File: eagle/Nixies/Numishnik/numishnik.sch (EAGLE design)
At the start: 74 parts, among them IC2 78L05F, IC5 74141N, IC6 DS3234, IC7 MEGA8-AI, Q1 IRF630N, SW1 BUTTON-IT_1181, T1 BTA92, T13 BTA42, T2 BTA42, T3 BTA92, T4 BTA42, T5 BTA92, T6 BTA42, T7 BTA92, T8 BTA42, X3 53047-06

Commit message: added IV-16 Numishnik
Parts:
- removed 220: (no value), rcl:CPOL-EUD/7343-31R
- removed C10: 10uF, rcl:CPOL-EUSMCB
- removed C100: 10uF/250V, rcl:CPOL-EUE5-13
- removed C12: 1.0, rcl:C-EUC0805S
- removed C6: 100/24V, rcl:CPOL-EUE3.5-8
- removed DOT1, DOT2, PAD1, PAD2: (no value), wirepad:1,6/0,8
- removed IC5: 74141N, 74xx-eu:74141N
- removed J2: (no value), 0-svo:DCJ-SMALL
- removed Q1: IRF630N, transistor-power:IRF740
- removed R14: (no value), 0-svo:RES4
- removed R18, R22, R26, R30: 2.4K, rcl:R-EU_R0805S
- removed R19, R23, R27, R31: 27K, rcl:R-EU_R0805S
- removed R21, R25, R29: 91K, rcl:R-EU_R0805S
- removed R4: 000, rcl:R-EU_R0805S
- removed S1, S2: (no value), switch-omron:31-XX
- removed SV1, SV2: (no value), con-lsta:FE20-1
- removed T1, T3, T5, T7: BTA92, transistor:MMBTA92LT1-PNP-SOT23-BEC
- removed T13, T2, T4, T6, T8: BTA42, transistor:MMBTA42LT1-NPN-SOT23-BEC
- removed U$1, U$2, U$3, U$4: IN-14, 0-nixies-russian:IN-14
- added C3: 10uF, rcl:CPOL-EUSMCB
- added IC1: MBI5026GP, 0-macroblock:MBI5026GP
- added N1, N2, N3, N4: IV-16, 0-nixies-russian:IV-16
- added R12, R13: 000, rcl:R-EU_R0805S
- added TP1, TP2: TPSPAD1-13, 0-svo:TPSPAD1-13
- added X1: USB-MICROB, SparkFun:USB-MICROB
- C2: value 33nF -> 10uF; device rcl:C-EUC0805S -> rcl:CPOL-EUSMCB
- D1: value 31DF6 -> BZX84C 3.3V; device diode:RGP30 -> diode:BZX84CSMD
- D2: value BAT54C -> BZX84C 3.3V; device diode:DIODE-2AC|CASOT23 -> diode:BZX84CSMD
- D3: value BAT54S -> 1N4004; device diode:DIODE_2CACA-SOT23 -> diode:1N4004
- IC2: value 78L05F -> MBI5026GP; device linear:78L05F -> 0-macroblock:MBI5026GP
- R1: value 91K -> 820
- R10: value 27K -> 10
- R11, R7, R8: value 1K -> 10
- R17: value 91K -> 2K2
- R2: value 470K -> 820
- R3: value 4K7 -> 100
- R6, R9: value 1K -> 100
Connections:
- net N$53 renamed RTCVCC
- removed net +UB: C6.+, IC2.VI, J2.1, PAD2.P
- removed net C0: IC5A.0, SV1.1, SV2.1, U$1.0, U$2.0, U$3.0, U$4.0
- removed net C1: IC5A.1, SV1.2, SV2.2, U$1.1, U$2.1, U$3.1, U$4.1
- removed net C2: IC5A.2, SV1.3, SV2.3, U$1.2, U$2.2, U$3.2, U$4.2
- removed net C3: IC5A.3, SV1.4, SV2.4, U$1.3, U$2.3, U$3.3, U$4.3
- removed net C4: IC5A.4, SV1.5, SV2.5, U$1.4, U$2.4, U$3.4, U$4.4
- removed net C5: IC5A.5, SV1.16, SV2.16, U$1.5, U$2.5, U$3.5, U$4.5
- removed net C6: IC5A.6, SV1.17, SV2.17, U$1.6, U$2.6, U$3.6, U$4.6
- removed net C7: IC5A.7, SV1.18, SV2.18, U$1.7, U$2.7, U$3.7, U$4.7
- removed net C8: IC5A.8, SV1.19, SV2.19, U$1.8, U$2.8, U$3.8, U$4.8
- removed net C9: IC5A.9, SV1.20, SV2.20, U$1.9, U$2.9, U$3.9, U$4.9
- removed net D0: IC5A.A, IC7.PC3(ADC3)
- removed net D1: IC5A.B, IC7.PC1(ADC1)
- removed net D2: IC5A.C, IC7.PC0(ADC0)
- removed net D3: IC5A.D, IC7.PC2(ADC2)
- removed net FBACK: C12.1, D3.AC, IC7.ADC7, R2.2, R3.2
- removed net HV+: C100.+, D1.C, R10.2, R18.2, R2.1, R22.2, R26.2, R30.2, SV1.6, SV2.6, T1.E, T3.E, T5.E, T7.E
- removed net HVPUMP: C2.2, IC7.PB1(OC1A)
- removed net N$10 (its old number): R19.1, U$1.A
- removed net N$15: R9.2, T6.B
- removed net N$16: R25.2, R26.1, T5.B
- removed net N$17: R25.1, T6.C
- removed net N$18: R27.2, T5.C
- removed net N$19: R23.1, U$2.A
- removed net N$20: R11.2, T8.B
- removed net N$21: R6.1, T13.B
- removed net N$22: R29.2, R30.1, T7.B
- removed net N$23: R29.1, T8.C
- removed net N$24: R31.2, T7.C
- removed net N$25: R27.1, U$3.A
- removed net N$26: R17.2, R18.1, T1.B
- removed net N$31: IC7.PD7(AIN1), R14.2.1
- removed net N$32: IC7.PD6(AIN0), R14.3.1
- removed net N$34: IC7.PD5(T1), R14.4.1
- removed net N$35: IC7.PB0(ICP), R14.1.1
- removed net N$39: R17.1, T2.C
- removed net N$51: DOT1.P, T13.C
- removed net N$6 (its old number): R19.2, T1.C
- removed net SA1: R14.1.2, R7.1, SV1.7, SV2.7
- removed net SA2: R14.2.2, R8.1, SV1.10, SV2.10
- removed net SA3: R14.3.2, R9.1, SV1.13, SV2.13
- removed net SA4: R11.1, R14.4.2, SV1.15, SV2.15
- new net D+: IC7.PD2(INT0), R3.1
- new net D-: IC7.PD3(INT1), R6.1
- new net LE: IC1.LE, IC2.LE, IC7.PC0(ADC0)
- new net MOSI#2: IC1.SDO, IC2.SDI
- new net N$2: R9.2, TP2.PP
- new net SEG0: IC1.OUT6#, N1.2
- new net SEG1: IC1.OUT5#, N1.3
- new net SEG10: IC1.OUT11#, N2.5
- new net SEG11: IC1.OUT10#, N2.6
- new net SEG12: IC1.OUT9#, N2.7
- new net SEG13: IC1.OUT8#, N2.8
- new net SEG14: IC2.OUT6#, N3.2
- new net SEG15: IC2.OUT5#, N3.3
- new net SEG16: IC2.OUT4#, N3.4
- new net SEG17: IC2.OUT3#, N3.5
- new net SEG18: IC2.OUT2#, N3.6
- new net SEG19: IC2.OUT1#, N3.7
- new net SEG2: IC1.OUT4#, N1.4
- new net SEG20: IC2.OUT0#, N3.8
- new net SEG21: IC2.OUT14#, N4.2
- new net SEG22: IC2.OUT13#, N4.3
- new net SEG23: IC2.OUT12#, N4.4
- new net SEG24: IC2.OUT11#, N4.5
- new net SEG25: IC2.OUT10#, N4.6
- new net SEG26: IC2.OUT9#, N4.7
- new net SEG27: IC2.OUT8#, N4.8
- new net SEG3: IC1.OUT3#, N1.5
- new net SEG4: IC1.OUT2#, N1.6
- new net SEG5: IC1.OUT1#, N1.7
- new net SEG6: IC1.OUT0#, N1.8
- new net SEG7: IC1.OUT14#, N2.2
- new net SEG8: IC1.OUT13#, N2.3
- new net SEG9: IC1.OUT12#, N2.4
- net +5V: now also C2.+, C3.+, D3.A, IC1.VDD, IC2.VDD, R17.1, X1.VBUS; no longer 220.+, C10.+, D3.C, IC2.VO, IC5P.VCC
- net BTN+: no longer S1.P
- net BTNSET: no longer S2.P
- net DOT: now also IC2.OUT15#, TP1.PP; no longer IC7.PD3(INT1), R4.1, R4.2, R6.2, SV1.12, SV2.12
- net GND: now also C2.-, C3.-, D1.A, D2.A, IC1.GND, IC1.OE#, IC2.OE#, R1.2, R2.2, X1.GND; no longer 220.-, C10.-, C100.-, C12.2, C6.-, D2.A1, D2.A2, D3.A, IC2.GND@1, IC5P.GND, J2.2, J2.3, Q1.S, R1.1, R3.1, S1.S, S2.S, SV1.14, SV1.8, SV1.9, SV2.14, SV2.8, SV2.9, T13.E, T2.E, T4.E, T6.E, T8.E
- net MOSI: now also IC1.SDI, R13.1, R13.2
- net N$11: now also N2.1, R8.2; no longer R21.2, R22.1, T3.B
- net N$12: now also N3.1, R10.2; no longer R21.1, T4.C
- net N$13: now also N4.1, R11.2; no longer R23.2, T3.C
- net N$14: now also D3.C, R10.1, R11.1, R7.1, R8.1, R9.1; no longer R31.1, U$4.A
- net N$3: now also N1.1, R7.2; no longer C2.1, D2.C, Q1.G, R1.2
- net N$4: now also IC1.R-EXT, R1.1; no longer DOT2.P, R10.1
- net N$5: now also IC2.R-EXT, R2.1; no longer R7.2, T2.B
- net N$7: now also D1.C, R17.2, R6.2, X1.D-; no longer D1.A, PAD1.P, Q1.D
- net N$8: now also D2.C, R3.2, X1.D+; no longer R8.2, T4.B
- net SCK: now also IC1.CLK, IC2.CLK, R12.1, R12.2
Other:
- note removed: "100uH"
- note removed: "A Nixie Clock by"
- note removed: "HV Boost converter"
- note removed: "MAIN BOARD"
- note removed: "SATASHNIK"
- note removed: "Setup Buttons"
- note removed: "St.Petersburg 2009-2010"
- note removed: "Viacheslav Slavinsky"
- note removed: "http://sensi.org/~svo"
- note removed: "low ESR"
- note removed: "recommended upgrade IRFB4620"
- moved on the sheet: BAT+, BAT-, C11, C13, C14, C5, COMGND, COMRXD, COMTXD, D4, IC6, IC7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

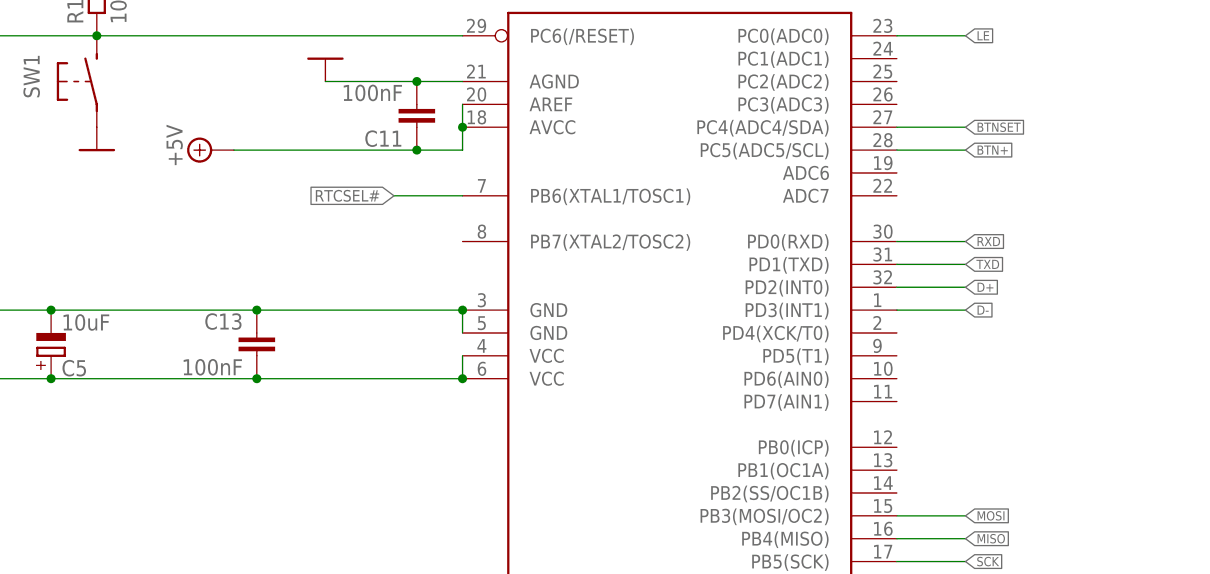
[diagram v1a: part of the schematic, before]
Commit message: added xtal, changed rtcsel#.. not routed
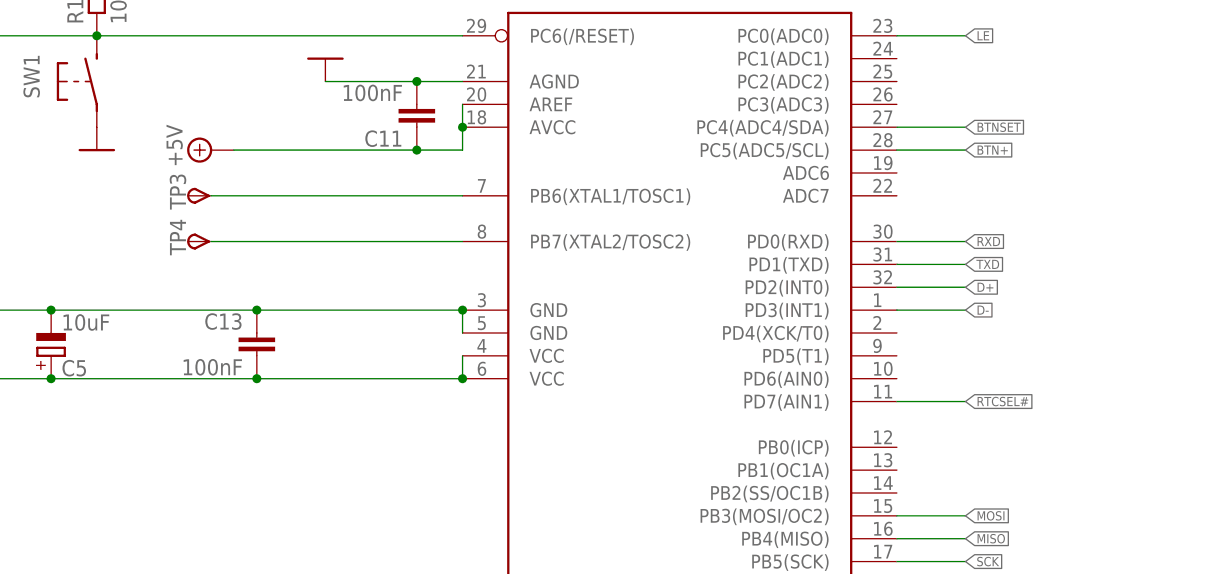
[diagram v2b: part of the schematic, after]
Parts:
- added TP3, TP4: TPSPAD1-13, 0-svo:TPSPAD1-13
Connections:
- new net N$1: IC7.PB6(XTAL1/TOSC1), TP3.PP
- new net XTAL2: IC7.PB7(XTAL2/TOSC2), TP4.PP
- net RTCSEL#: now also IC7.PD7(AIN1); no longer IC7.PB6(XTAL1/TOSC1)
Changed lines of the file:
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@@
 <grid distance="0.1" unitdist="inch" unit="inch" style="lines" multiple="1" display="no" altdistance="0.01" altunitdist="inch" altunit="inch"/>
 <layers>
-<layer number="1" name="Top" color="4" fill="1" visible="yes" active="no"/>
-<layer number="16" name="Bottom" color="1" fill="1" visible="yes" active="no"/>
-<layer number="17" name="Pads" color="2" fill="1" visible="yes" active="no"/>
-<layer number="18" name="Vias" color="2" fill="1" visible="yes" active="no"/>
-<layer number="19" name="Unrouted" color="6" fill="1" visible="yes" active="no"/>
-<layer number="20" name="Dimension" color="15" fill="1" visible="yes" active="no"/>
-<layer number="21" name="tPlace" color="7" fill="1" visible="yes" active="no"/>
-<layer number="22" name="bPlace" color="7" fill="1" visible="yes" active="no"/>
-<layer number="23" name="tOrigins" color="15" fill="1" visible="yes" active="no"/>
-<layer number="24" name="bOrigins" color="15" fill="1" visible="yes" active="no"/>
-<layer number="25" name="tNames" color="7" fill="1" visible="yes" active="no"/>
-<layer number="26" name="bNames" color="7" fill="1" visible="yes" active="no"/>
-<layer number="27" name="tValues" color="7" fill="1" visible="yes" active="no"/>
-<layer number="28" name="bValues" color="7" fill="1" visible="yes" active="no"/>
+<layer number="1" name="Top" color="4" fill="1" visible="no" active="no"/>
+<layer number="16" name="Bottom" color="1" fill="1" visible="no" active="no"/>
+<layer number="17" name="Pads" color="2" fill="1" visible="no" active="no"/>
+<layer number="18" name="Vias" color="2" fill="1" visible="no" active="no"/>
+<layer number="19" name="Unrouted" color="6" fill="1" visible="no" active="no"/>
+<layer number="20" name="Dimension" color="15" fill="1" visible="no" active="no"/>
+<layer number="21" name="tPlace" color="7" fill="1" visible="no" active="no"/>
+<layer number="22" name="bPlace" color="7" fill="1" visible="no" active="no"/>
+<layer number="23" name="tOrigins" color="15" fill="1" visible="no" active="no"/>
+<layer number="24" name="bOrigins" color="15" fill="1" visible="no" active="no"/>
+<layer number="25" name="tNames" color="7" fill="1" visible="no" active="no"/>
+<layer number="26" name="bNames" color="7" fill="1" visible="no" active="no"/>
+<layer number="27" name="tValues" color="7" fill="1" visible="no" active="no"/>
+<layer number="28" name="bValues" color="7" fill="1" visible="no" active="no"/>
 <layer number="29" name="tStop" color="7" fill="3" visible="no" active="no"/>
 <layer number="30" name="bStop" color="7" fill="6" visible="no" active="no"/>
@@
 <layer number="35" name="tGlue" color="7" fill="4" visible="no" active="no"/>
 <layer number="36" name="bGlue" color="7" fill="5" visible="no" active="no"/>
-<layer number="37" name="tTest" color="7" fill="1" visible="yes" active="no"/>
-<layer number="38" name="bTest" color="7" fill="1" visible="yes" active="no"/>
+<layer number="37" name="tTest" color="7" fill="1" visible="no" active="no"/>
+<layer number="38" name="bTest" color="7" fill="1" visible="no" active="no"/>
 <layer number="39" name="tKeepout" color="4" fill="11" visible="no" active="no"/>
 <layer number="40" name="bKeepout" color="1" fill="11" visible="no" active="no"/>
@@
 <layer number="44" name="Drills" color="7" fill="1" visible="no" active="no"/>
 <layer number="45" name="Holes" color="7" fill="1" visible="no" active="no"/>
-<layer number="46" name="Milling" color="3" fill="1" visible="yes" active="no"/>
-<layer number="47" name="Measures" color="7" fill="1" visible="yes" active="no"/>
-<layer number="48" name="Document" color="7" fill="1" visible="yes" active="no"/>
-<layer number="49" name="Reference" color="7" fill="1" visible="yes" active="no"/>
-<layer number="50" name="dxf" color="7" fill="1" visible="yes" active="no"/>
-<layer number="51" name="tDocu" color="7" fill="1" visible="yes" active="no"/>
-<layer number="52" name="bDocu" color="7" fill="1" visible="yes" active="no"/>
-<layer number="53" name="tGND_GNDA" color="7" fill="9" visible="yes" active="no"/>
-<layer number="54" name="bGND_GNDA" color="1" fill="9" visible="yes" active="no"/>
-<layer number="56" name="wert" color="7" fill="1" visible="yes" active="no"/>
+<layer number="46" name="Milling" color="3" fill="1" visible="no" active="no"/>
+<layer number="47" name="Measures" color="7" fill="1" visible="no" active="no"/>
+<layer number="48" name="Document" color="7" fill="1" visible="no" active="no"/>
+<layer number="49" name="Reference" color="7" fill="1" visible="no" active="no"/>
+<layer number="50" name="dxf" color="7" fill="1" visible="no" active="no"/>
+<layer number="51" name="tDocu" color="7" fill="1" visible="no" active="no"/>
+<layer number="52" name="bDocu" color="7" fill="1" visible="no" active="no"/>
+<layer number="53" name="tGND_GNDA" color="7" fill="9" visible="no" active="no"/>
+<layer number="54" name="bGND_GNDA" color="1" fill="9" visible="no" active="no"/>
+<layer number="56" name="wert" color="7" fill="1" visible="no" active="no"/>
 <layer number="91" name="Nets" color="2" fill="1" visible="yes" active="yes"/>
 <layer number="92" name="Busses" color="1" fill="1" visible="yes" active="yes"/>
@@
 <part name="GND3" library="supply1" deviceset="GND" device=""/>
 <part name="GND5" library="supply1" deviceset="GND" device=""/>
+<part name="TP3" library="0-svo" deviceset="TPS" device="PAD1-13"/>
+<part name="TP4" library="0-svo" deviceset="TPS" device="PAD1-13"/>
 </parts>
 <sheets>
@@
 <instance part="GND3" gate="1" x="218.44" y="193.04" smashed="yes"/>
 <instance part="GND5" gate="1" x="279.4" y="193.04" smashed="yes"/>
+<instance part="TP3" gate="G$1" x="58.42" y="193.04" rot="R90"/>
+<instance part="TP4" gate="G$1" x="58.42" y="187.96" rot="R90"/>
 </instances>
 <busses>
@@
 <net name="RTCSEL#" class="0">
 <segment>
-<wire x1="88.9" y1="193.04" x2="81.28" y2="193.04" width="0.1524" layer="91"/>
-<label x="81.28" y="193.04" size="1.27" layer="95" rot="R180" xref="yes"/>
-<pinref part="IC7" gate="G$1" pin="PB6(XTAL1/TOSC1)"/>
-</segment>
-<segment>
 <wire x1="27.94" y1="30.48" x2="17.78" y2="30.48" width="0.1524" layer="91"/>
 <label x="17.78" y="30.48" size="1.016" layer="95" rot="R180" xref="yes"/>
 <pinref part="IC6" gate="G$1" pin="CS#"/>
+</segment>
+<segment>
+<pinref part="IC7" gate="G$1" pin="PD7(AIN1)"/>
+<wire x1="137.16" y1="170.18" x2="144.78" y2="170.18" width="0.1524" layer="91"/>
+<label x="144.78" y="170.18" size="1.016" layer="95" xref="yes"/>
 </segment>
 </net>
@@
 </segment>
 </net>
+<net name="XTAL2" class="0">
+<segment>
+<pinref part="IC7" gate="G$1" pin="PB7(XTAL2/TOSC2)"/>
+<pinref part="TP4" gate="G$1" pin="PP"/>
+<wire x1="88.9" y1="187.96" x2="60.96" y2="187.96" width="0.1524" layer="91"/>
+</segment>
+</net>
+<net name="N$1" class="0">
+<segment>
+<pinref part="IC7" gate="G$1" pin="PB6(XTAL1/TOSC1)"/>
+<pinref part="TP3" gate="G$1" pin="PP"/>
+<wire x1="88.9" y1="193.04" x2="60.96" y2="193.04" width="0.1524" layer="91"/>
+</segment>
+</net>

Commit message: latest version, not all fixes fully fixed: careful with SS
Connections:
- removed net BTN+: IC7.PC5(ADC5/SCL)
- removed net BTNSET: IC7.PC4(ADC4/SDA)
- net +5V: no longer IC7.AREF
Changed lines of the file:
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@@
 <wire x1="88.9" y1="198.12" x2="83.82" y2="198.12" width="0.1524" layer="91"/>
 <wire x1="88.9" y1="198.12" x2="88.9" y2="200.66" width="0.1524" layer="91"/>
-<wire x1="88.9" y1="200.66" x2="88.9" y2="203.2" width="0.1524" layer="91"/>
 <junction x="83.82" y="198.12"/>
-<junction x="88.9" y="200.66"/>
 <pinref part="C11" gate="G$1" pin="1"/>
 <pinref part="V2" gate="+5V" pin="+5V"/>
 <pinref part="IC7" gate="G$1" pin="AVCC"/>
-<pinref part="IC7" gate="G$1" pin="AREF"/>
 </segment>
 <segment>
@@
 </segment>
 </net>
-<net name="BTNSET" class="0">
-<segment>
-<wire x1="137.16" y1="200.66" x2="144.78" y2="200.66" width="0.1524" layer="91"/>
-<label x="144.78" y="200.66" size="1.016" layer="95" rot="MR180" xref="yes"/>
-<pinref part="IC7" gate="G$1" pin="PC4(ADC4/SDA)"/>
-</segment>
-</net>
-<net name="BTN+" class="0">
-<segment>
-<wire x1="144.78" y1="198.12" x2="137.16" y2="198.12" width="0.1524" layer="91"/>
-<label x="144.78" y="198.12" size="1.016" layer="95" xref="yes"/>
-<pinref part="IC7" gate="G$1" pin="PC5(ADC5/SCL)"/>
-</segment>
-</net>
